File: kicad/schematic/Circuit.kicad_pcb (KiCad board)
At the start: 2 copper layers, 70 parts, among them Q1 AO3400A, Q2 AO3400A, Q3 AO3400A, Q4 AO3400A, Q5 AO3400A, Q6 AO3400A, Q7 AO3400A, Q8 AO3400A

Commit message: almost final - text image missing
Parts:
- removed BAT+1, BAT-1: ~, ESP_global:blank pad
- added REF**: MountingHole_2.1mm, MountingHole:MountingHole_2.1mm, F.Cu at (100.8, 87.6)
- added REF**: MountingHole_2.1mm, MountingHole:MountingHole_2.1mm, F.Cu at (30.7, 87.6)
- added REF**: MountingHole_2.1mm, MountingHole:MountingHole_2.1mm, F.Cu at (100.8, 37.8)
- added REF**: MountingHole_2.1mm, MountingHole:MountingHole_2.1mm, F.Cu at (31.0, 37.6)
- added U3: JST-PH2, Connector_JST:JST_EH_S2B-EH_1x02_P2.50mm_Horizontal, F.Cu at (38.3, 64.0)
- moved ESP32_S3_ZERO1 3.82 mm to (45.7, 47.5)
- moved R17 1.40 mm to (49.1, 65.8)
- moved R18 1.40 mm to (54.2, 65.8)
- moved R19 1.40 mm to (58.9, 65.8)
- moved O3962A 0.64 mm to (45.2, 76.7)
- renumbered U2 to HW-085, U1 to O3962A, RGB-DIN1 to RGB-DIN, RGB-VDD1 to RGB-VDD, RGB-gnd1 to RGB-gnd, R1 to RL1, Switch1 to Sw1, Switch2 to Sw2, m7+1 to m+, m8+1 to m+, m3+1 to m+, m6+1 to m+, m4+1 to m+, m2+1 to m+, m1+1 to m+, m1-1 to m-, m7-1 to m-, m3-1 to m-, m2-1 to m-, m4-1 to m-, m8-1 to m-, m6-1 to m-, m5+1 to m5+, m5-1 to m5-
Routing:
- net GND: track 154.1 -> 8.07 mm, vias 19 -> 10
- net Net-(ESP32_S3_ZERO1-GP12): track 41.0 -> 60.4 mm, vias 2 -> 6
- net Net-(D1-K): track 170.9 -> 155.6 mm, vias 15 -> 19
- net Net-(ESP32_S3_ZERO1-5V): track 94.9 -> 80.0 mm, vias 10 -> 6
- net Net-(ESP32_S3_ZERO1-GP10): track 25.1 -> 32.0 mm, vias 0 -> 4
- net Net-(ESP32_S3_ZERO1-GP11): track 44.2 -> 50.5 mm, vias 3 -> 6
- net Net-(RGB-DIN1-pin): track 38.1 -> 32.6 mm, vias 6 -> 2
- net Net-(ESP32_S3_ZERO1-GP1): track 17.3 -> 21.9 mm, vias 2 -> 4
- net Net-(ESP32_S3_ZERO1-GP6): track 16.6 -> 12.9 mm
- net Net-(ESP32_S3_ZERO1-GP13): track 38.3 -> 41.9 mm, vias 0 -> 6
- net Net-(ESP32_S3_ZERO1-GP5): track 13.8 -> 16.9 mm, vias 2 -> 4
- net Net-(Switch1-pin): track 20.5 -> 22.9 mm, vias 1 -> 2
- net Net-(BT1--): track 36.0 -> 34.0 mm
- net Net-(BT1-+): track 31.4 -> 29.5 mm, vias 1 -> 2
- net Net-(ESP32_S3_ZERO1-GP9): track 26.6 -> 25.3 mm
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- added copper zone on B.Cu, net GND
- added copper zone on F.Cu, net GND
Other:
- board outline added: 75 x 55 mm
- board text added: "JLCJLCJLCJLC"

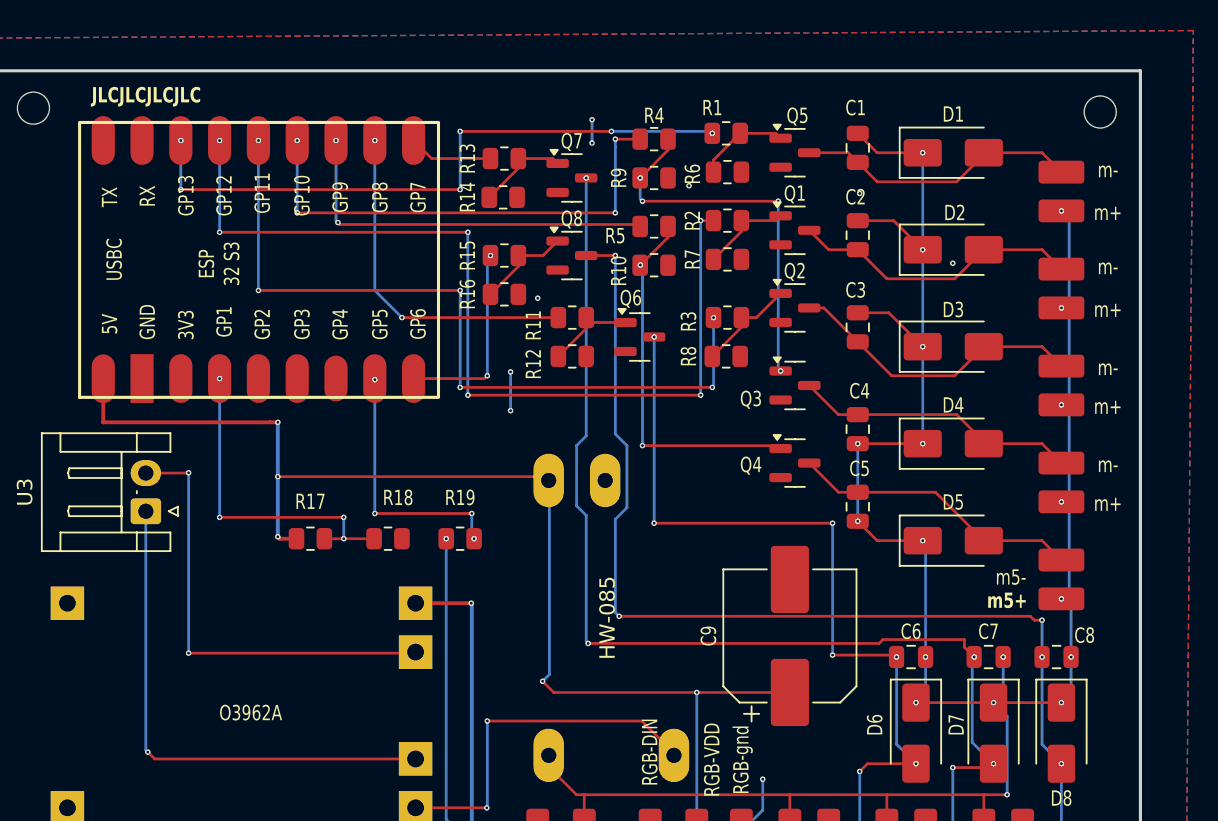
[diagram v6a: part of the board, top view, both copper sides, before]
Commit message: hopefully last push - m5 fixed, logo + text added
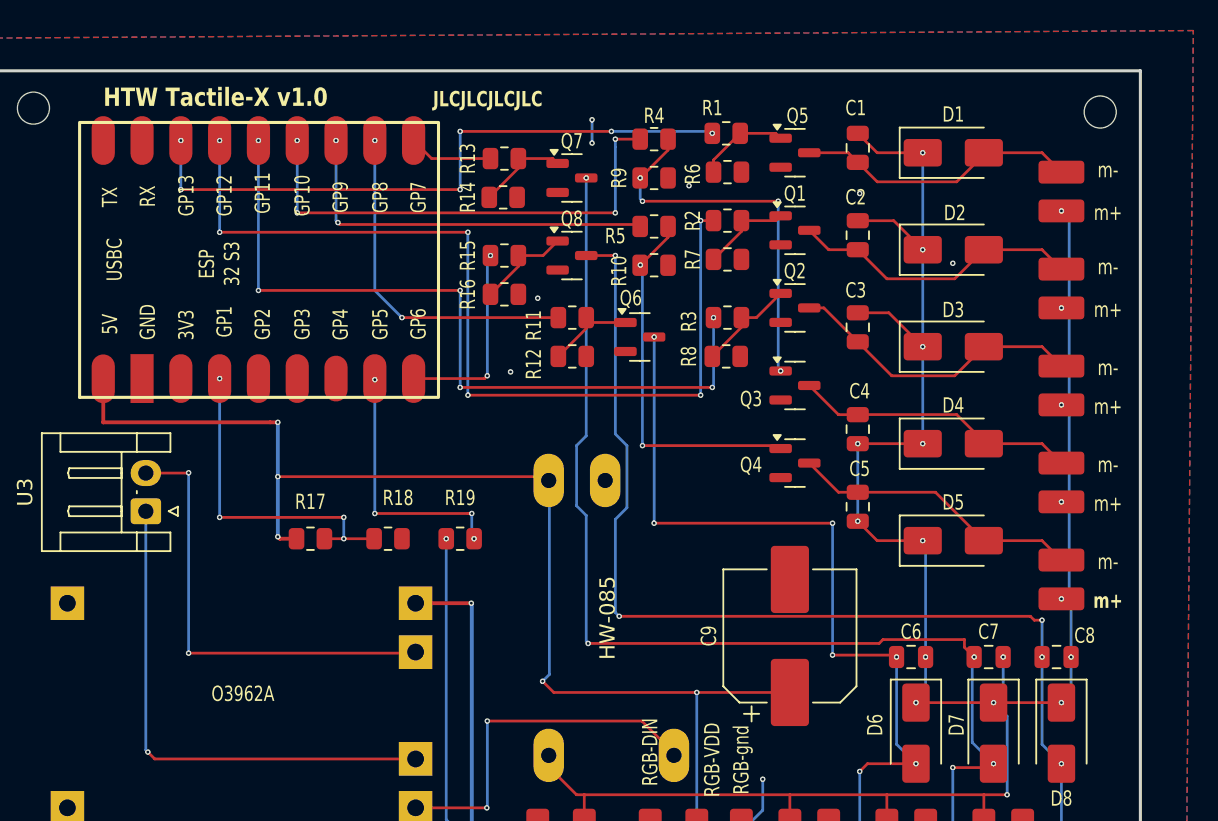
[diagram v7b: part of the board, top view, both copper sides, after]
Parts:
- added G***: LOGO, Graphics:logo, B.Cu at (45.0, 76.5)
- renumbered m5+ to m+, m5- to m-
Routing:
- net GND: track 8.07 -> 5.53 mm, vias 10 -> 9
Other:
- board text added: "HTW Tactile-X v1.0"
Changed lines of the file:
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@@
 		(layer "F.Cu")
 		(at 98.298 67.183 -90)
-		(property "Reference" "m5-"
-			(at 1.143 3.302 0)
+		(property "Reference" "m-"
+			(at 0.127 -3.048 0)
 			(unlocked yes)
 			(layer "F.SilkS")
@@
 		(at 45.212 76.708 180)
 		(property "Reference" "O3962A"
-			(at 0 -0.5 0)
+			(at 0.508 0.762 0)
 			(unlocked yes)
 			(layer "F.SilkS")
@@
 		(layer "F.Cu")
 		(at 98.298 69.723 -90)
-		(property "Reference" "m5+"
-			(at 0.127 3.556 0)
+		(property "Reference" "m+"
+			(at 0.127 -3.048 0)
 			(unlocked yes)
 			(layer "F.SilkS")
@@
 		)
 	)
+	(footprint "Graphics:logo"
+		(layer "B.Cu")
+		(at 44.958 76.454 180)
+		(property "Reference" "G***"
+			(at 4.318 -0.872102 0)
+			(layer "F.SilkS")
+			(hide yes)
+			(effects
+				(font
+					(size 1.5 1.5)
+					(thickness 0.3)
+				)
+				(justify mirror)
+			)
+		)
+		(property "Value" "LOGO"
+			(at 0.75 0 0)
+			(layer "B.SilkS")
+			(hide yes)
+			(effects
+				(font
+					(size 1.5 1.5)
+					(thickness 0.3)
+				)
+				(justify mirror)
+			)
+		)
+		(property "Datasheet" ""
+			(at 0 0 0)
+			(layer "B.Fab")
+			(hide yes)
+			(effects
+				(font
+					(size 1.27 1.27)
+					(thickness 0.15)
+				)
+				(justify mirror)
+			)
+		)
+		(property "Description" ""
+			(at 0 0 0)
+			(layer "B.Fab")
+			(hide yes)
+			(effects
+				(font
+					(size 1.27 1.27)
+					(thickness 0.15)
+				)
+				(justify mirror)
+			)
+		)
+		(attr board_only exclude_from_pos_files exclude_from_bom)
+		(fp_poly
+			(pts
+				(xy -5.66867 7.412876) (xy -5.66867 6.976825) (xy -6.104721 6.976825) (xy -6.540773 6.976825) (xy -6.540773 7.412876)
+				(xy -6.540773 7.848928) (xy -6.104721 7.848928) (xy -5.66867 7.848928)
+			)
+			(stroke
+				(width 0)
+				(type solid)
+			)
+			(fill yes)
+			(layer "B.SilkS")
+		)
+		(fp_poly
+			(pts
+				(xy -6.540773 8.284979) (xy -6.540773 7.848928) (xy -6.976824 7.848928) (xy -7.412876 7.848928)
+				(xy -7.412876 8.284979) (xy -7.412876 8.721031) (xy -6.976824 8.721031) (xy -6.540773 8.721031)
+			)
+			(stroke
+				(width 0)
+				(type solid)
+			)
+			(fill yes)
+			(layer "B.SilkS")
+		)
+		(fp_poly
+			(pts
+				(xy -6.540773 5.232619) (xy -6.540773 4.360516) (xy -6.976824 4.360516) (xy -7.412876 4.360516)
+				(xy -7.412876 5.232619) (xy -7.412876 6.104722) (xy -6.976824 6.104722) (xy -6.540773 6.104722)
+			)
+			(stroke
+				(width 0)
+				(type solid)
+			)
+			(fill yes)
+			(layer "B.SilkS")
+		)
+		(fp_poly
+			(pts
+				(xy -5.66867 -2.180257) (xy -5.66867 -3.488411) (xy -5.232618 -3.488411) (xy -4.796567 -3.488411)
+				(xy -4.796567 -6.10472) (xy -4.796567 -8.721029) (xy -6.104721 -8.721029) (xy -7.412876 -8.721029)
+				(xy -7.412876 -6.10472) (xy -7.412876 -3.488411) (xy -6.976824 -3.488411) (xy -6.540773 -3.488411)
+				(xy -6.540773 -2.180257) (xy -6.540773 -0.872102) (xy -6.104721 -0.872102) (xy -5.66867 -0.872102)
+			)
+			(stroke
+				(width 0)
+				(type solid)
+			)
+			(fill yes)
+			(layer "B.SilkS")
+		)
+		(fp_poly
+			(pts
+				(xy -1.308155 5.66867) (xy -1.308155 4.360516) (xy -0.872103 4.360516) (xy -0.436052 4.360516) (xy -0.436052 5.232619)
+				(xy -0.436052 6.104722) (xy 0 6.104722) (xy 0.436051 6.104722) (xy 0.436051 6.540773) (xy 0.436051 6.976825)
+				(xy 0.872103 6.976825) (xy 1.308154 6.976825) (xy 1.308154 5.66867) (xy 1.308154 4.360516) (xy 0.872103 4.360516)
+				(xy 0.436051 4.360516) (xy 0.436051 3.924464) (xy 0.436051 3.488413) (xy 0.872103 3.488413) (xy 1.308154 3.488413)
+				(xy 1.308154 -0.872102) (xy 1.308154 -5.232617) (xy 3.488412 -5.232617) (xy 5.668669 -5.232617)
+				(xy 5.668669 -5.668669) (xy 5.668669 -6.10472) (xy 6.104721 -6.10472) (xy 6.540772 -6.10472) (xy 6.540772 -6.540772)
+				(xy 6.540772 -6.976823) (xy 6.104721 -6.976823) (xy 5.668669 -6.976823) (xy 5.668669 -7.412875)
+				(xy 5.668669 -7.848926) (xy 6.104721 -7.848926) (xy 6.540772 -7.848926) (xy 6.540772 -7.412875)
+				(xy 6.540772 -6.976823) (xy 6.976824 -6.976823) (xy 7.412875 -6.976823) (xy 7.412875 -7.412875)
+				(xy 7.412875 -7.848926) (xy 6.976824 -7.848926) (xy 6.540772 -7.848926) (xy 6.540772 -8.284978)
+				(xy 6.540772 -8.721029) (xy 4.360515 -8.721029) (xy 2.180257 -8.721029) (xy 2.180257 -8.284978)
+				(xy 2.180257 -7.848926) (xy 0.872103 -7.848926) (xy -0.436052 -7.848926) (xy -0.436052 -8.284978)
+				(xy -0.436052 -8.721029) (xy -0.872103 -8.721029) (xy -1.308155 -8.721029) (xy -1.308155 -8.284978)
+				(xy -1.308155 -7.848926) (xy -2.180258 -7.848926) (xy -3.052361 -7.848926) (xy -3.052361 -8.284978)
+				(xy -3.052361 -8.721029) (xy -3.488412 -8.721029) (xy -3.924464 -8.721029) (xy -3.924464 -8.284978)
+				(xy -3.924464 -7.848926) (xy -3.488412 -7.848926) (xy -3.052361 -7.848926) (xy -3.052361 -7.412875)
+				(xy -3.052361 -6.976823) (xy 2.180257 -6.976823) (xy 2.180257 -7.848926) (xy 2.616309 -7.848926)
+				(xy 3.05236 -7.848926) (xy 3.05236 -6.976823) (xy 3.924463 -6.976823) (xy 3.924463 -7.848926) (xy 4.360515 -7.848926)
+				(xy 4.796566 -7.848926) (xy 4.796566 -6.976823) (xy 4.796566 -6.10472) (xy 4.360515 -6.10472) (xy 3.924463 -6.10472)
+				(xy 3.924463 -6.976823) (xy 3.05236 -6.976823) (xy 3.05236 -6.10472) (xy 2.616309 -6.10472) (xy 2.180257 -6.10472)
+				(xy 2.180257 -6.976823) (xy -3.052361 -6.976823) (xy -3.488412 -6.976823) (xy -3.924464 -6.976823)
+				(xy -3.924464 -3.05236) (xy -3.052361 -3.05236) (xy -3.052361 -5.232617) (xy -2.180258 -5.232617)
+				(xy -1.308155 -5.232617) (xy -1.308155 -3.05236) (xy -1.308155 -0.872102) (xy -2.180258 -0.872102)
+				(xy -3.052361 -0.872102) (xy -3.052361 -3.05236) (xy -3.924464 -3.05236) (xy -3.924464 -2.616308)
+				(xy -3.924464 1.744207) (xy -5.66867 1.744207) (xy -7.412876 1.744207) (xy -7.412876 2.61631) (xy -7.412876 3.488413)
+				(xy -6.540773 3.488413) (xy -5.66867 3.488413) (xy -5.66867 3.052361) (xy -5.66867 2.61631) (xy -4.796567 2.61631)
+				(xy -3.924464 2.61631) (xy -3.924464 3.052361) (xy -3.052361 3.052361) (xy -3.052361 2.61631) (xy -2.616309 2.61631)
+				(xy -2.180258 2.61631) (xy -2.180258 3.052361) (xy -1.308155 3.052361) (xy -1.308155 2.61631) (xy -0.872103 2.61631)
+				(xy -0.436052 2.61631) (xy -0.436052 3.052361) (xy -0.436052 3.488413) (xy -0.872103 3.488413) (xy -1.308155 3.488413)
+				(xy -1.308155 3.052361) (xy -2.180258 3.052361) (xy -2.180258 3.488413) (xy -2.616309 3.488413)
+				(xy -3.052361 3.488413) (xy -3.052361 3.052361) (xy -3.924464 3.052361) (xy -3.924464 3.488413)
+				(xy -3.488412 3.488413) (xy -3.052361 3.488413) (xy -3.052361 4.796567) (xy -3.052361 6.104722)
+				(xy -2.616309 6.104722) (xy -2.180258 6.104722) (xy -2.180258 6.540773) (xy -2.180258 6.976825)
+				(xy -1.744206 6.976825) (xy -1.308155 6.976825)
+			)
+			(stroke
+				(width 0)
+				(type solid)
+			)
+			(fill yes)
+			(layer "B.SilkS")
+		)
+		(embedded_fonts no)
+	)
 	(gr_rect
 		(start 28.468 35.148)
@@
 		)
 	)
+	(gr_text "HTW Tactile-X v1.0"
+		(at 35.56 37.592 0)
+		(layer "F.SilkS")
+		(effects
+			(font
+				(size 1.2 1)
+				(thickness 0.2)
+				(bold yes)
+			)
+			(justify left bottom)
+		)
+	)
 	(gr_text "R1"
 		(at 75.438 37.592 0)
@@
 	)
 	(gr_text "JLCJLCJLCJLC"
-		(at 34.798 37.338 0)
+		(at 57.15 37.592 0)
 		(layer "F.SilkS")
 		(effects
@@
 	)
 	(via
-		(at 62.23 57.404)
-		(size 0.36)
-		(drill 0.18)
-		(layers "F.Cu" "B.Cu")
-		(free yes)
-		(net 15)
-	)
-	(via
 		(at 73.914 42.672)
 		(size 0.36)
@@
 		(width 0.18)
 		(layer "B.Cu")
-		(net 15)
-	)
-	(segment
-		(start 62.23 54.864)
-		(end 62.23 57.404)
-		(width 0.18)
-		(layer "B.Cu")
